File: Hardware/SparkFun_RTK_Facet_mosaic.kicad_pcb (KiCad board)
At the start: 4 copper layers, 59.5 x 43 mm, 157 parts, among them J1 U.FL_SMD, J2 JST_2mm_LiPo, J3 Qwiic_RA, J5 Conn_01x12_FPC_0.5mm, J6 Conn_01x12_FPC_0.5mm, J7 Conn_01x12_FPC_0.5mm, Q1 MBT3904DW1, Q2 SIL2308, Q3 BSS138, U1 ESP32-WROVER-E-N16R8, U10 MCP73833_MSOP, U11 AP2112K-3.3, U12 STLQ015-3.3, U13 74HC4052D, U2 mosaic-X5, U3 CH340C, U4 MAX17048, U5 AP2112K-3.3, U9 USB251xB, Y1 24MHz

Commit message: Add missing PROD_IDs
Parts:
- TR1: value Val** -> RFCMF1220100M4T
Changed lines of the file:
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@@
     (at 115.062 136.398 -90)
     (descr "ESP-WROOM-32D\n<br>\n<br>\nThis version of the module contains an onboard trace-antenna connector. \n<br>\nIt is virtually identical to the onboard u.FL version (ESP32-WROOM-32U), \n<br>\nexcept it is slightly longer and requires the keepout zone.")
-    (property "PROD_ID" "IC-")
+    (property "PROD_ID" "IC-21314")
     (property "Sheetfile" "SparkFun_RTK_Facet_mosaic.kicad_sch")
     (property "Sheetname" "")
@@
   (footprint "SparkFun-Connector:FPC_12_0.5MM" (layer "F.Cu")
     (at 122.35 115.4 180)
+    (property "PROD_ID" "CONN-15766")
     (property "Sheetfile" "SparkFun_RTK_Facet_mosaic.kicad_sch")
     (property "Sheetname" "")
@@
   (footprint "SparkFun-Connector:FPC_12_0.5MM" (layer "F.Cu")
     (at 113.35 115.4 180)
+    (property "PROD_ID" "CONN-15766")
     (property "Sheetfile" "SparkFun_RTK_Facet_mosaic.kicad_sch")
     (property "Sheetname" "")
@@
   (footprint "SparkFun-Connector:FPC_12_0.5MM" (layer "F.Cu")
     (at 140.35 115.4 180)
+    (property "PROD_ID" "CONN-15766")
     (property "Sheetfile" "SparkFun_RTK_Facet_mosaic.kicad_sch")
     (property "Sheetname" "")
@@
         (effects (font (size 0.5 0.5) (thickness 0.1) bold) (justify mirror))
     )
-    (fp_text value "Val**" (at 0 -1.2) (layer "B.Fab")
+    (fp_text value "RFCMF1220100M4T" (at 0 -1.2) (layer "B.Fab")
         (effects (font (size 0.5 0.5) (thickness 0.1) bold) (justify mirror))
     )

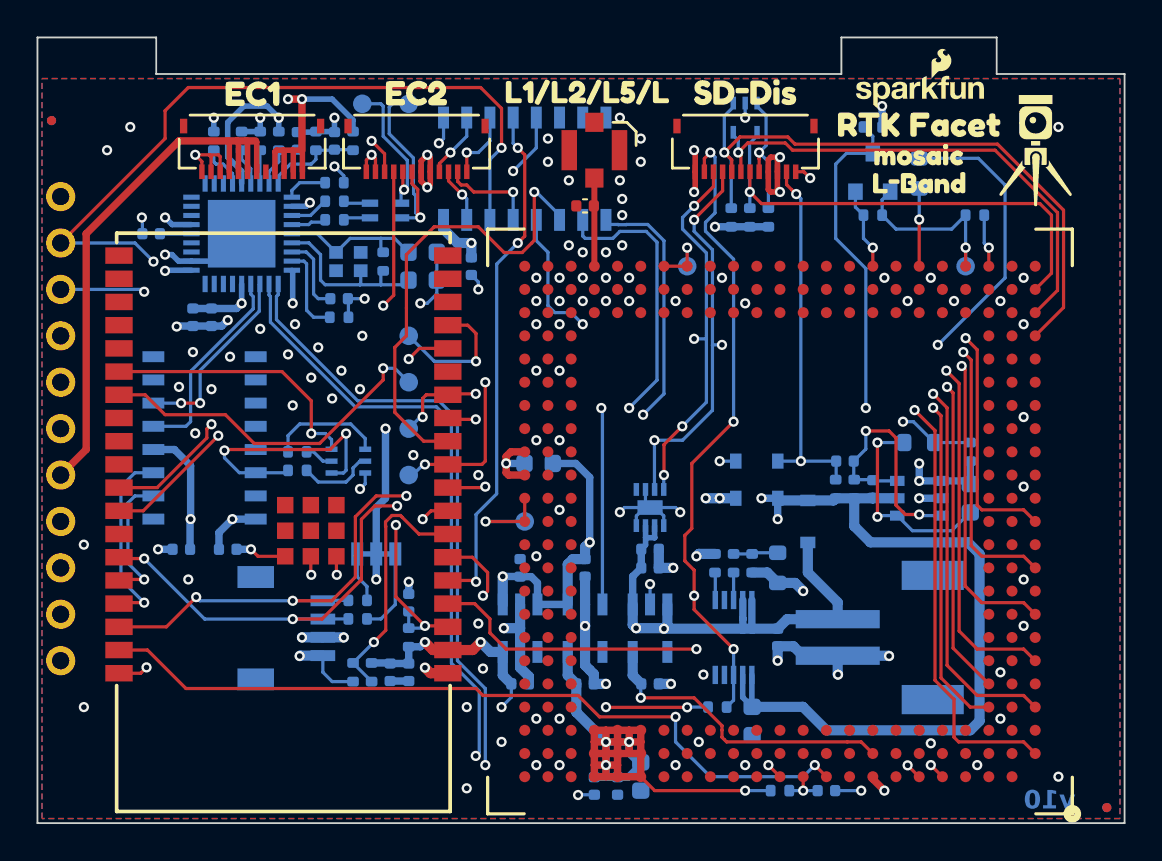
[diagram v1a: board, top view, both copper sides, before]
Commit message: Add extra Test Points
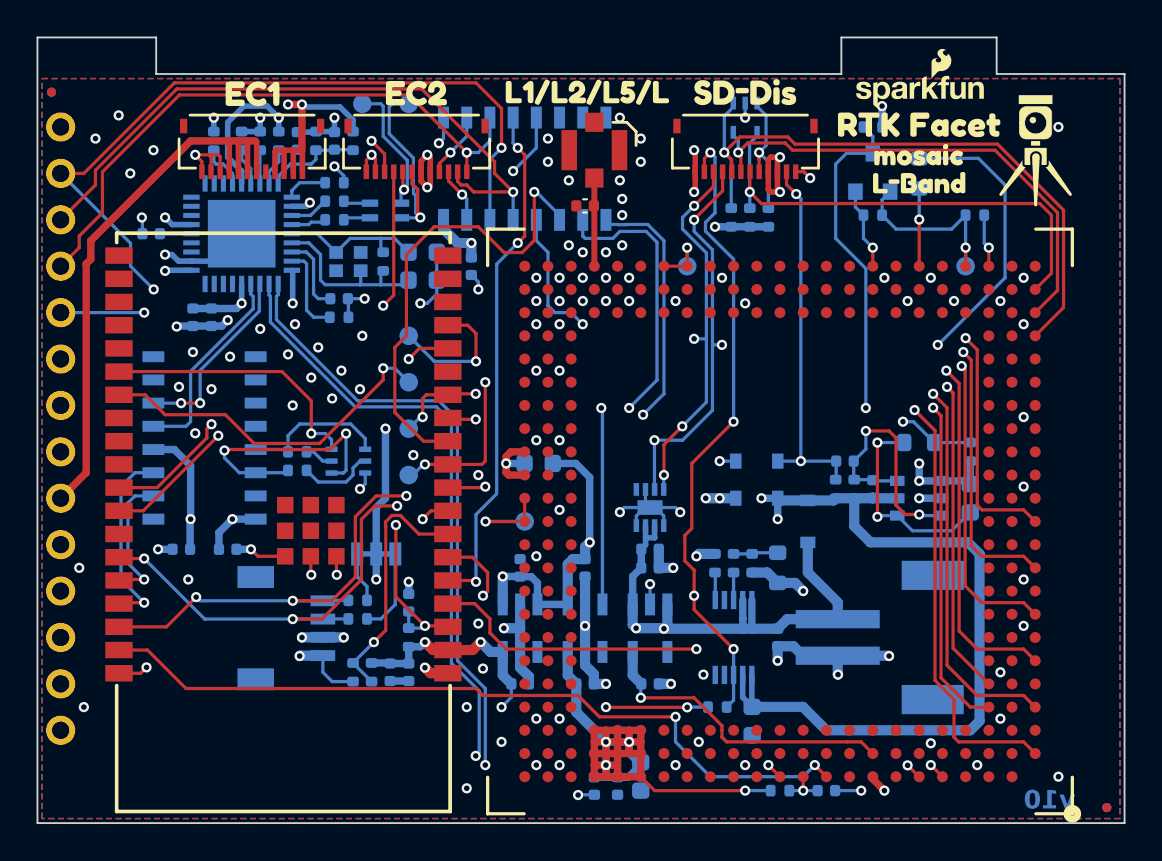
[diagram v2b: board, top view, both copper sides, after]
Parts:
- removed kibuzzard-65A7F4A9: G***, kibuzzard-65A7F4A9
- added TP21: PTH, SparkFun-Connector:1X01, F.Cu at (102.9, 119.4)
- added TP22: PTH, SparkFun-Connector:1X01, F.Cu at (102.9, 121.9)
- added TP23: PTH, SparkFun-Connector:1X01, F.Cu at (102.9, 147.3)
- added kibuzzard-65A7F440: G***, kibuzzard-65A7F440, B.Cu at (105.4, 147.3)
- added kibuzzard-65AEA1E6: G***, kibuzzard-65AEA1E6, B.Cu at (105.5, 119.4)
- added kibuzzard-65AEA201: G***, kibuzzard-65AEA201, B.Cu at (105.0, 121.9)
- added kibuzzard-65AEA759: G***, kibuzzard-65AEA759, B.Cu at (105.3, 127.0)
- moved TP4 3.81 mm to (102.9, 114.3)
- moved TP6 3.81 mm to (102.9, 116.8)
- moved kibuzzard-65A7F440 3.81 mm to (105.4, 114.3)
- moved kibuzzard-65A7F47C 3.81 mm to (105.2, 116.8)
- moved FID2 1.56 mm to (102.4, 112.4)
- moved FID3 1.56 mm to (102.4, 112.4)
- moved TP1 1.27 mm to (102.9, 137.2)
- moved TP10 1.27 mm to (102.9, 144.8)
- moved TP12 1.27 mm to (102.9, 132.1)
- moved TP8 1.27 mm to (102.9, 134.6)
- moved TP9 1.27 mm to (102.9, 142.2)
- moved kibuzzard-65A7F4D6 1.27 mm to (105.4, 132.1)
- moved kibuzzard-65A7F4E8 1.27 mm to (105.4, 134.6)
- moved kibuzzard-65A7F511 1.27 mm to (105.3, 137.2)
- moved kibuzzard-65A7F565 1.27 mm to (105.3, 142.2)
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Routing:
- net ExternalDATA_TXO: track 5.34 -> 36.2 mm
- net ExternalDATA_RXI: track 3.86 -> 33.0 mm
- net ESP~{RST}: track 37.6 -> 36.4 mm
- net MPPS_3V3: track 108.8 -> 108.0 mm
- net POWER_BTN: track 68.1 -> 67.6 mm
- net M_BACKUP: track 59.1 -> 58.6 mm
- net VBATT: track 62.9 -> 62.3 mm
- net 3.3V: track 119.8 -> 120.3 mm
- net VIN: track 89.0 -> 88.5 mm
- net 3.3V_P: track 206.1 -> 205.6 mm
- net GND: vias 126 -> 128

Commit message: Final tweaks
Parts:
- TR1: value RFCMF1220100M4T -> Val**
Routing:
- net ESP26/DAC2: track 25.8 -> 28.8 mm
- net MOSAIC_DM: track 59.9 -> 61.3 mm
- net MOSAIC_DP: track 61.5 -> 62.4 mm
- net ESP14/MRX1: track 53.3 -> 52.6 mm
- net MEventA: track 52.1 -> 52.8 mm
- net ExternalDATA_TXO: track 36.2 -> 35.6 mm
- net ESP39/ADC39: track 28.3 -> 28.9 mm
- net GND: vias 128 -> 133

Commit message: Add RFCMF1220100M4T value
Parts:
- TR1: value Val** -> RFCMF1220100M4T
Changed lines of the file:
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@@
         (effects (font (size 0.5 0.5) (thickness 0.1) bold) (justify mirror))
     )
-    (fp_text value "Val**" (at 0 -1.2) (layer "B.Fab")
+    (fp_text value "RFCMF1220100M4T" (at 0 -1.2) (layer "B.Fab")
         (effects (font (size 0.5 0.5) (thickness 0.1) bold) (justify mirror))
     )
